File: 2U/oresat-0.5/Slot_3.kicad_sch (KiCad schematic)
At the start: 3 parts

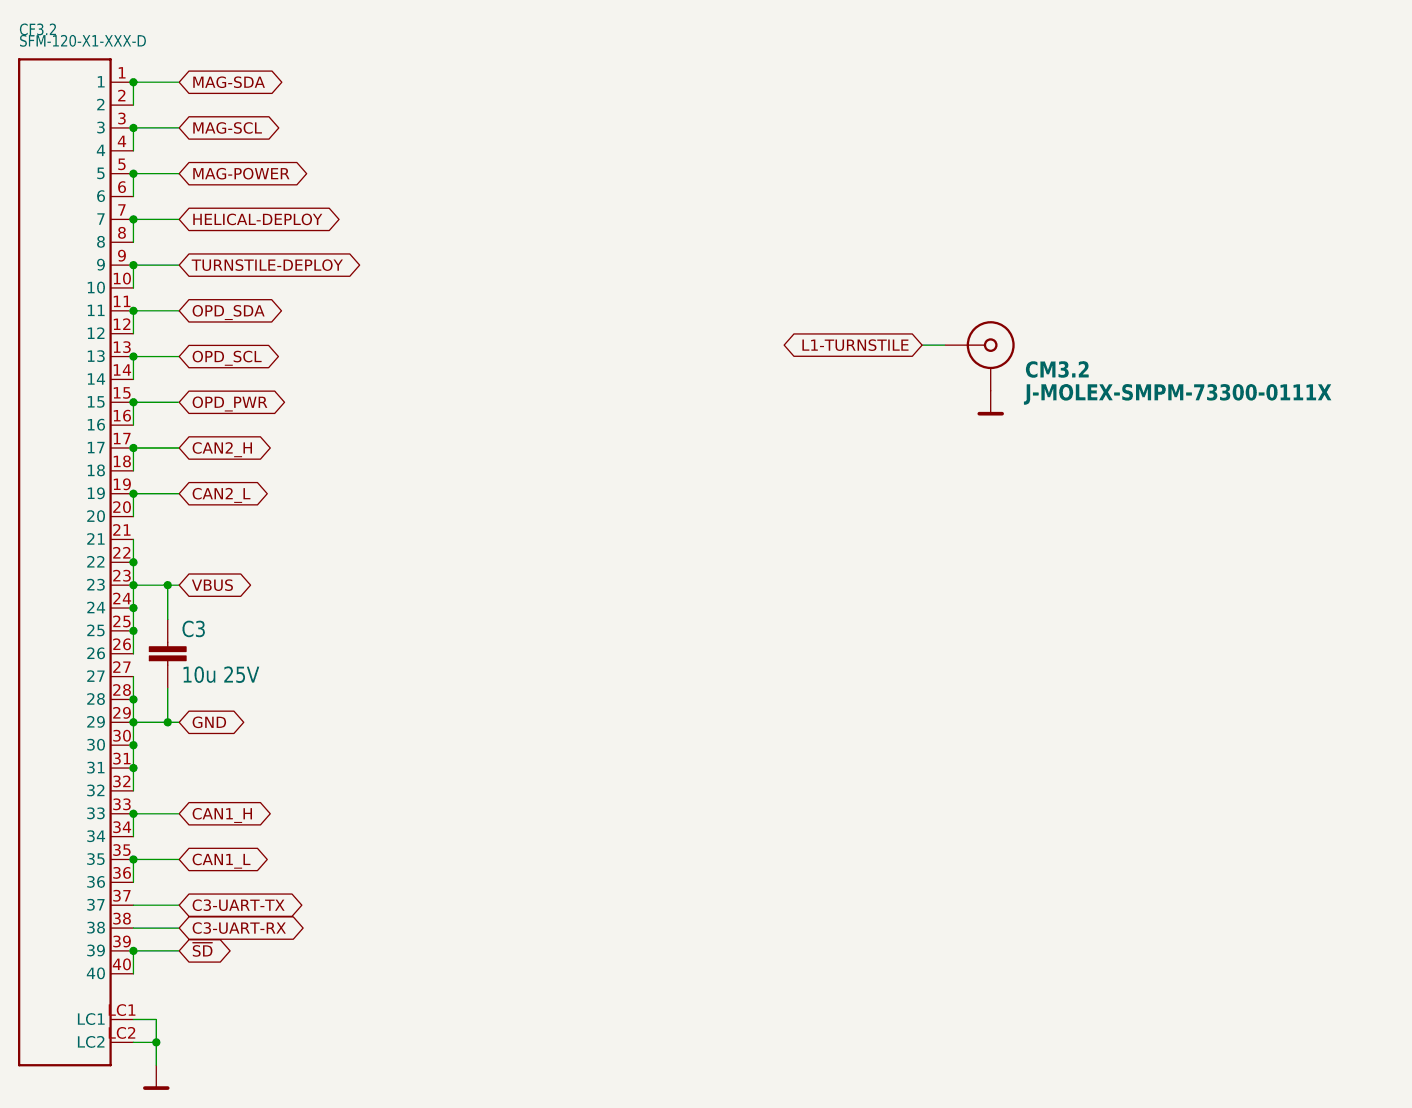
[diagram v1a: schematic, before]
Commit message: Fixed all (most) of the issues from Eagle imports
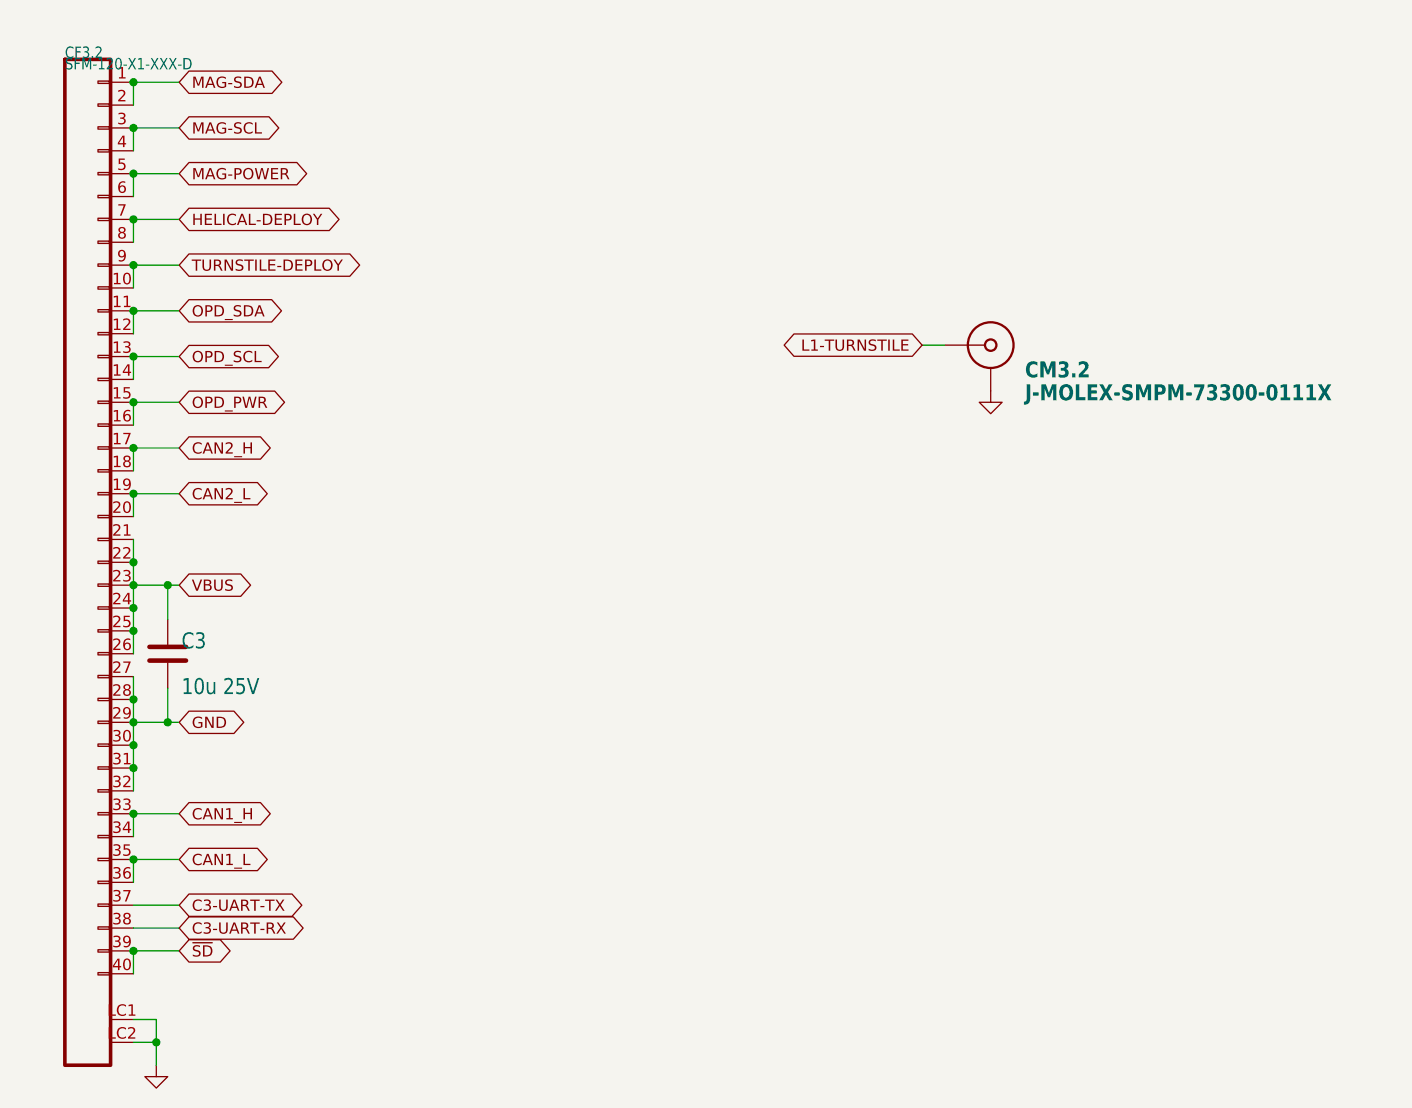
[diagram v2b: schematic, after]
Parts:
- C3: symbol oresat0-1u-backplane-eagle-import:C-EU1206-B -> Device:C
- CF3.2: symbol oresat-backplane-2u-eagle-import:SFM-120-X1-XXX-D -> oresat-connectors:J-SAMTEC-TFM-120-01-L-D-RA
- CM3.2: symbol oresat-symbols:J-MOLEX-SMPM-73300-0111X_1 -> oresat-connectors:J-MOLEX-SMPM-73300-0111X_1

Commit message: Moved entire schematic to single page
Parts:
- removed C3: 10u 25V, Capacitor_SMD:C_1206_3216Metric, symbol Device:C
- removed CF3.2: SFM-120-X1-XXX-D, oresat-connectors:J-SAMTEC-SFM-120-X1-XXX-D, symbol oresat-connectors:J-SAMTEC-TFM-120-01-L-D-RA
- removed CM3.2: J-MOLEX-SMPM-73300-0111X, oresat-connectors:J-MOLEX-SMPM-73300-0111X-long, symbol oresat-connectors:J-MOLEX-SMPM-73300-0111X_1
